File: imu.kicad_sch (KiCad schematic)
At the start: 4 parts, among them U3 IIS2MDCTR, U4 LSM6DSO32TR, U5 TMP108AIYFFR, U6 BME280

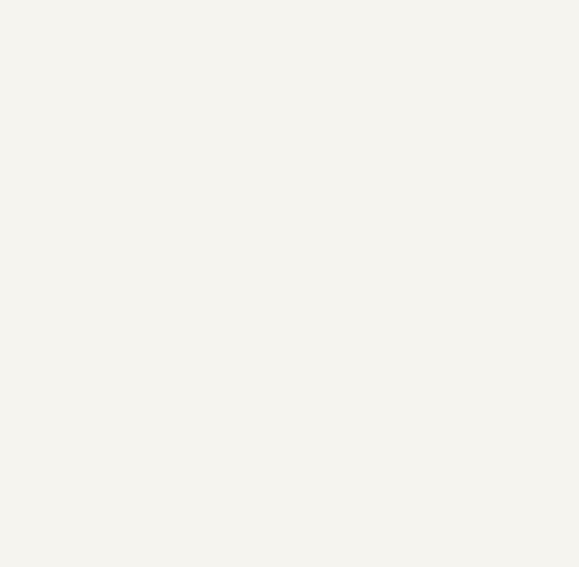
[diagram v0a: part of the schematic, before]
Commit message: [#94684] Add ports to subsheets
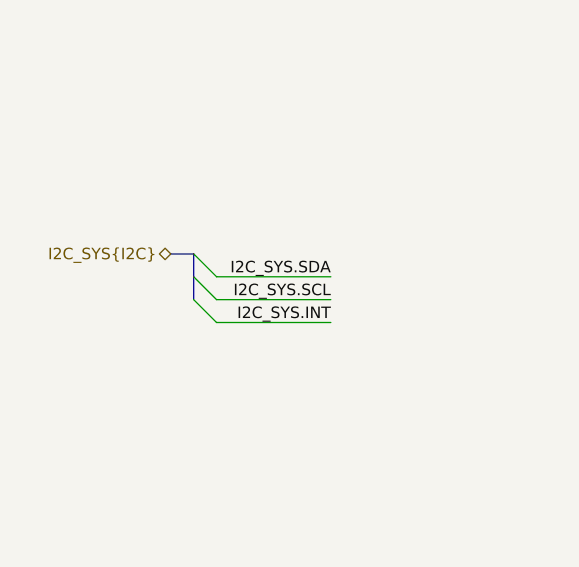
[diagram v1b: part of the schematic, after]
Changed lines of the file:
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@@
 	(generator "eeschema")
 	(generator_version "9.0")
-	(paper "A4")
+	(paper "A3")
 	(title_block
 		(title "renode-reference-platform")
@@
 		(company "Antmicro")
 	)
+	(bus_entry
+		(at 60.96 76.2)
+		(size 2.54 2.54)
+		(stroke
+			(width 0)
+			(type default)
+		)
+	)
+	(bus_entry
+		(at 60.96 78.74)
+		(size 2.54 2.54)
+		(stroke
+			(width 0)
+			(type default)
+		)
+	)
+	(bus_entry
+		(at 60.96 81.28)
+		(size 2.54 2.54)
+		(stroke
+			(width 0)
+			(type default)
+		)
+	)
+	(wire
+		(pts
+			(xy 63.5 78.74) (xy 76.2 78.74)
+		)
+		(stroke
+			(width 0)
+			(type default)
+		)
+	)
+	(wire
+		(pts
+			(xy 63.5 81.28) (xy 76.2 81.28)
+		)
+		(stroke
+			(width 0)
+			(type default)
+		)
+	)
+	(wire
+		(pts
+			(xy 63.5 83.82) (xy 76.2 83.82)
+		)
+		(stroke
+			(width 0)
+			(type default)
+		)
+	)
+	(bus
+		(pts
+			(xy 60.96 78.74) (xy 60.96 81.28)
+		)
+		(stroke
+			(width 0)
+			(type default)
+		)
+	)
+	(bus
+		(pts
+			(xy 60.96 76.2) (xy 60.96 78.74)
+		)
+		(stroke
+			(width 0)
+			(type default)
+		)
+	)
+	(bus
+		(pts
+			(xy 58.42 76.2) (xy 60.96 76.2)
+		)
+		(stroke
+			(width 0)
+			(type default)
+		)
+	)
+	(label "I2C_SYS.SDA"
+		(at 76.2 78.74 180)
+		(effects
+			(font
+				(size 1.27 1.27)
+			)
+			(justify right bottom)
+		)
+	)
+	(label "I2C_SYS.SCL"
+		(at 76.2 81.28 180)
+		(effects
+			(font
+				(size 1.27 1.27)
+			)
+			(justify right bottom)
+		)
+	)
+	(label "I2C_SYS.INT"
+		(at 76.2 83.82 180)
+		(effects
+			(font
+				(size 1.27 1.27)
+			)
+			(justify right bottom)
+		)
+	)
+	(hierarchical_label "I2C_SYS{I2C}"
+		(shape bidirectional)
+		(at 58.42 76.2 180)
+		(effects
+			(font
+				(size 1.27 1.27)
+			)
+			(justify right)
+		)
+	)
 	(symbol

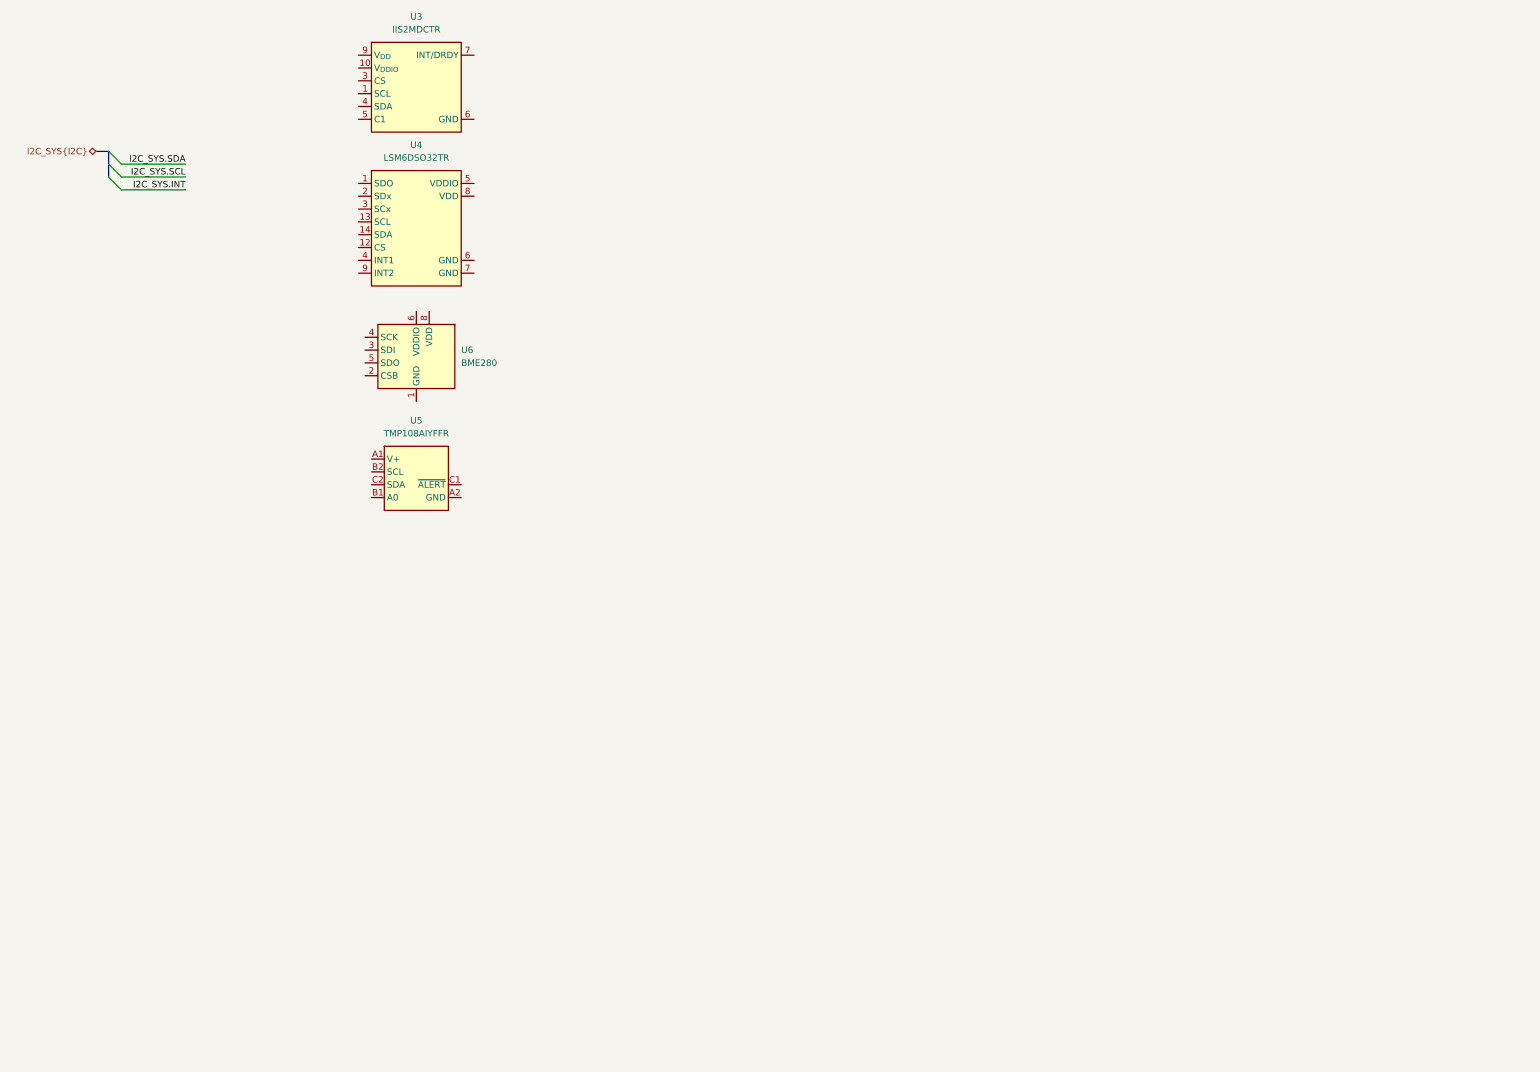
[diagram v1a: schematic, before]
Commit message: [#94940] Add magnetometer and acc+gyro
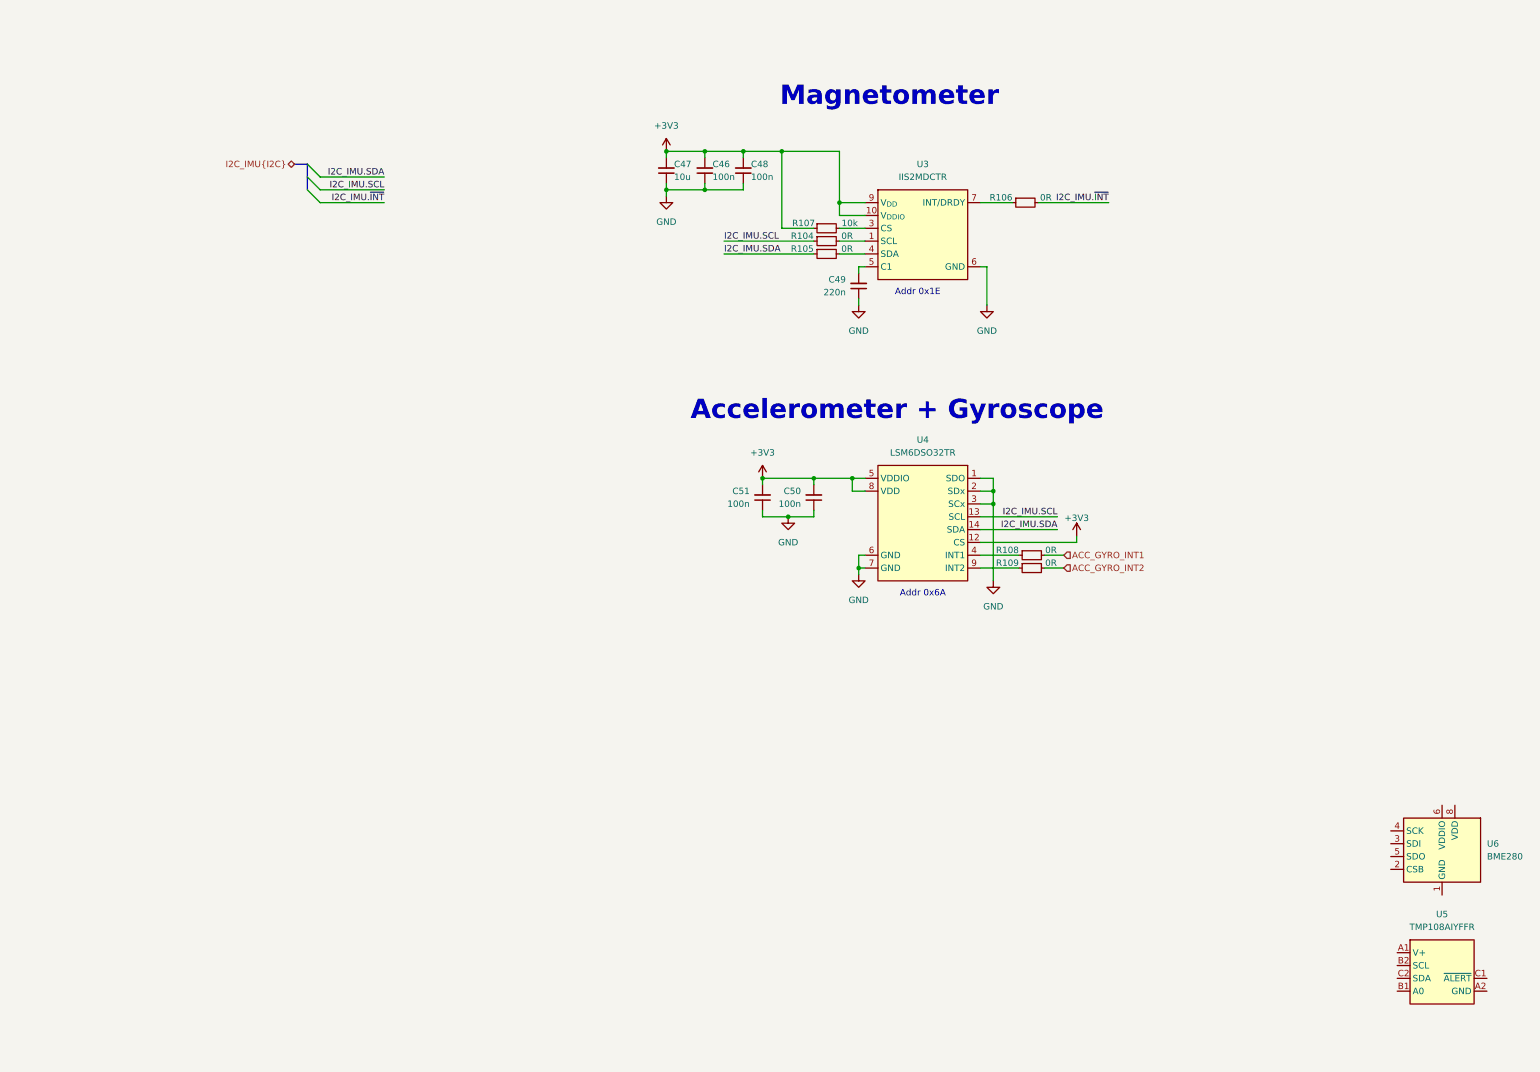
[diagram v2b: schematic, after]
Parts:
- added C46, C48, C50, C51: C_100n_0402, antmicro-footprints:C_0402_1005Metric, symbol antmicroCapacitors0402:C_100n_0402
- added C47: C_10u_0402, antmicro-footprints:C_0402_1005Metric, symbol antmicroCapacitors0402:C_10u_0402
- added C49: C_220n_0402, antmicro-footprints:C_0402_1005Metric, symbol antmicroCapacitors0402:C_220n_0402
- added R104, R105, R106, R108, R109: R_0R_0402, antmicro-footprints:R_0402_1005Metric, symbol antmicroResistors0402:R_0R_0402
- added R107: R_10k_0402, antmicro-footprints:R_0402_1005Metric, symbol antmicroResistors0402:R_10k_0402
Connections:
- net at U3.1 (SCL): now also R104.2
- net +3V3: now reaches U3.10 (V_{DDIO})
- net +3V3: now also U3.9 (V_{DD}), U4.12 (CS), U4.5 (VDDIO), U4.8 (VDD), C46.2, C47.2, C48.2, C50.2, C51.2, R107.1
- net at U3.3 (CS): now also R107.2
- net at U3.4 (SDA): now also R105.2
- net at U3.5 (C1): now also C49.2
- net GND: now reaches U3.6 (GND), U3.8 (GND)
- net GND: now also U4.1 (SDO), U4.2 (SDx), U4.3 (SCx), U4.6 (GND), U4.7 (GND), C46.1, C47.1, C48.1, C49.1, C50.1, C51.1
- net at U3.7 (INT/DRDY): now also R106.1
- net I2C_IMU.SCL: now reaches U4.13 (SCL)
- net I2C_IMU.SCL: now also R104.1
- net I2C_IMU.SDA: now reaches U4.14 (SDA)
- net I2C_IMU.SDA: now also R105.1
- net at U4.4 (INT1): now also R108.1
- net at U4.9 (INT2): now also R109.1
- new net ACC_GYRO_INT1: R108.2
- new net ACC_GYRO_INT2: R109.2
- new net I2C_IMU.~{INT}: R106.2
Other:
- note added: "Accelerometer + Gyroscope"
- note added: "Addr 0x1E"
- note added: "Addr 0x6A"
- note added: "Magnetometer"
- moved on the sheet: U3, U4, U5, U6

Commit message: [#94940] Add barometer and temperature sensors
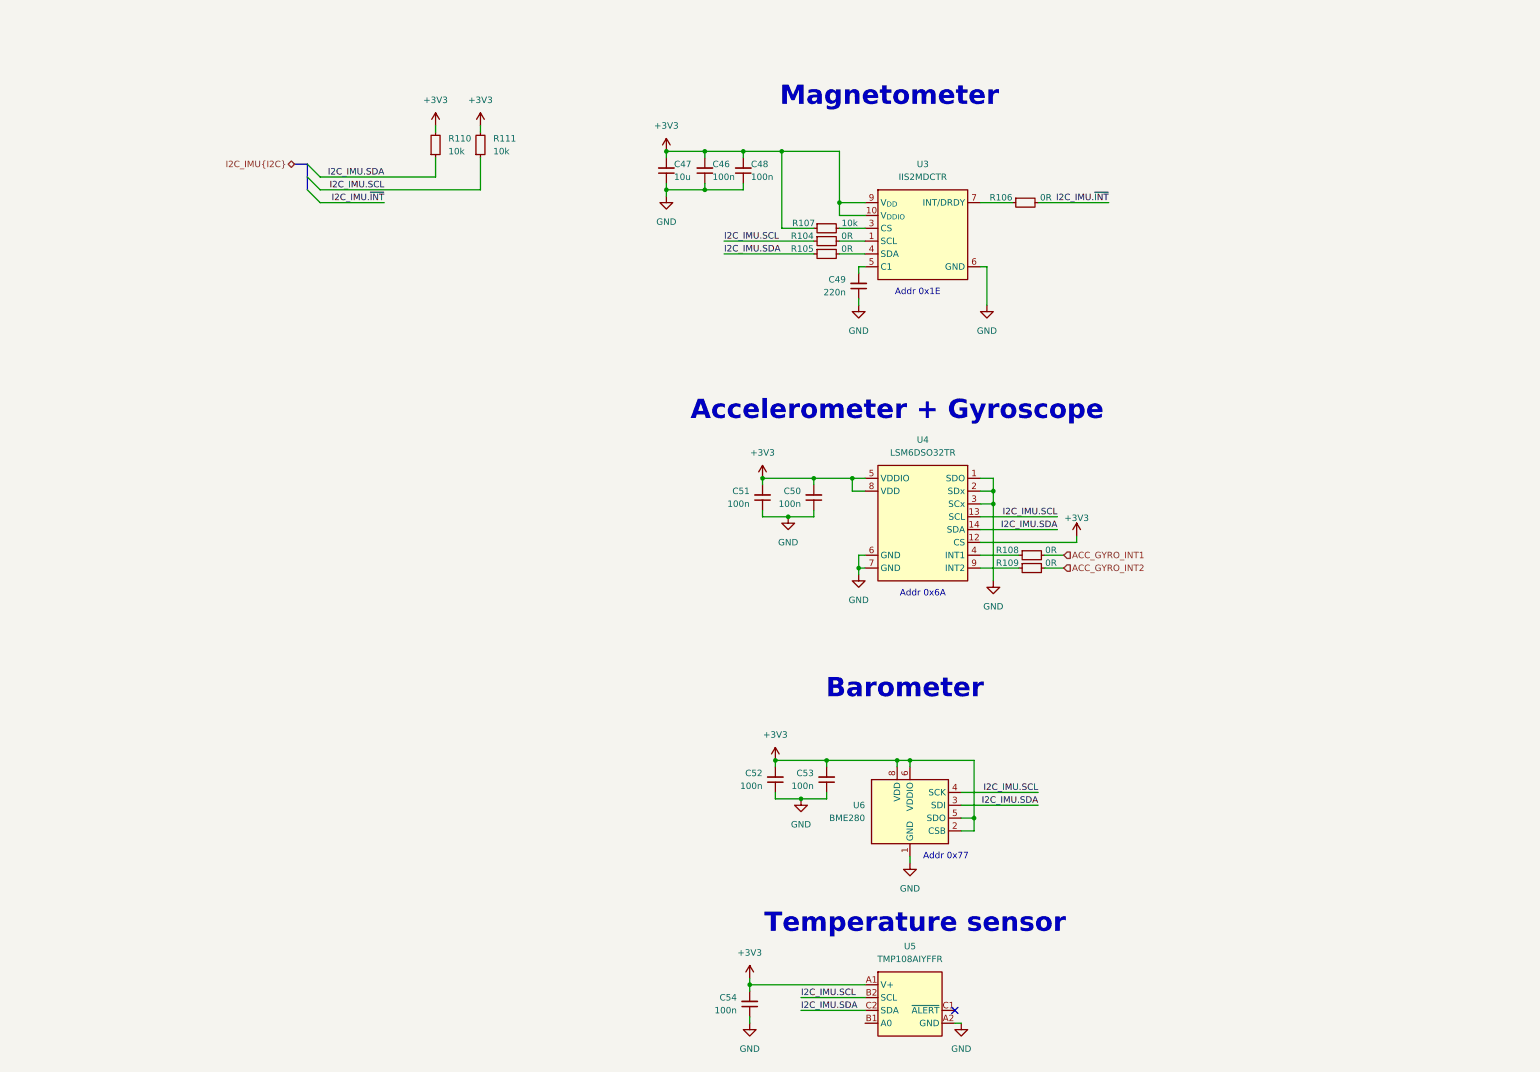
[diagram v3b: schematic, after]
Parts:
- added C52, C53, C54: C_100n_0402, antmicro-footprints:C_0402_1005Metric, symbol antmicroCapacitors0402:C_100n_0402
- added R110, R111: R_10k_0402, antmicro-footprints:R_0402_1005Metric, symbol antmicroResistors0402:R_10k_0402
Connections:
- net +3V3: now also U5.A1 (V+), U6.2 (CSB), U6.5 (SDO), U6.6 (VDDIO), U6.8 (VDD), C52.2, C53.2, C54.2, R110.2, R111.2
- net GND: now also U5.A2 (GND), U6.1 (GND), U6.7 (GND), C52.1, C53.1, C54.1
- net I2C_IMU.SCL: now also U5.B2 (SCL), U6.4 (SCK), R111.1
- net I2C_IMU.SDA: now also U5.C2 (SDA), U6.3 (SDI), R110.1
- no-connect marks 0 -> 1
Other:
- note added: "Addr 0x77"
- note added: "Barometer"
- note added: "Temperature sensor"
- moved on the sheet: U5, U6
